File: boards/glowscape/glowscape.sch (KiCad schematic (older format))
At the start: 47 parts, among them IC1 ATMEGA168-P, IC2 SN75176B, J1 JACK_2P, J2 RJ45, J3 RJ45, J4 JACK_STEREO, SW1 SW_PUSH, SW2 SW_PUSH, SW3 SW_PUSH, X1 XO-14S

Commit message: working on routing the boards
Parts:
- added C4: 10uF, symbol C
- C1: value 2.2uF -> 100uF
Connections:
- net GND: now also C4.2
- net VCC: now also C4.1
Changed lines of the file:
@@
-EESchema Schematic File Version 2  date Mon 06 Feb 2012 02:11:49 AM EST
+EESchema Schematic File Version 2  date Fri 17 Feb 2012 09:03:31 AM EST
 LIBS:power
 LIBS:device
@@
 LIBS:xo-14s
 LIBS:diy_connectors
-EELAYER 43  0
+LIBS:glowscape-cache
+EELAYER 25  0
 EELAYER END
 $Descr A4 11700 8267
@@
 Sheet 1 1
 Title ""
-Date "6 feb 2012"
+Date "17 feb 2012"
 Rev ""
 Comp ""
@@
 Comment4 ""
 $EndDescr
+Wire Wire Line
+	4050 4850 4050 4900
 Connection ~ 3750 4550
 Wire Wire Line
@@
 	3000 1250 2850 1250
 Connection ~ 3150 1150
-Wire Wire Line
-	4050 5350 4050 5600
 Connection ~ 4050 5450
 Wire Wire Line
@@
 	4000 3750 4000 4150
 Connection ~ 4000 3750
+Wire Wire Line
+	4050 5300 4050 5600
+Connection ~ 4050 5350
+$Comp
+L C C4
+U 1 1 4F3DFEBE
+P 4050 5100
+F 0 "C4" H 4000 5200 50  0000 L CNN
+F 1 "10uF" H 3950 5000 50  0000 L CNN
+	1    4050 5100
+	1    0    0    -1
+$EndComp
+$Comp
+L VCC #PWR01
+U 1 1 4F3DFEB2
+P 4050 4850
+F 0 "#PWR01" H 4050 4950 30  0001 C CNN
+F 1 "VCC" H 4050 4950 30  0000 C CNN
+	1    4050 4850
+	1    0    0    -1
+$EndComp
 $Comp
 L JACK_STEREO J4
@@
 $EndComp
 $Comp
-L GND #PWR?
+L GND #PWR02
 U 1 1 4F2F79CC
 P 3750 4600
-F 0 "#PWR?" H 3750 4600 30  0001 C CNN
+F 0 "#PWR02" H 3750 4600 30  0001 C CNN
 F 1 "GND" H 3750 4530 30  0001 C CNN
 	1    3750 4600
@@
 $EndComp
 $Comp
-L GND #PWR?
+L GND #PWR03
 U 1 1 4F2F7860
 P 4800 2850
-F 0 "#PWR?" H 4800 2850 30  0001 C CNN
+F 0 "#PWR03" H 4800 2850 30  0001 C CNN
 F 1 "GND" H 4800 2780 30  0001 C CNN
 	1    4800 2850
@@
 $EndComp
 $Comp
-L VCC #PWR?
+L VCC #PWR04
 U 1 1 4F2F785B
 P 4800 2350
-F 0 "#PWR?" H 4800 2450 30  0001 C CNN
+F 0 "#PWR04" H 4800 2450 30  0001 C CNN
 F 1 "VCC" H 4800 2450 30  0000 C CNN
 	1    4800 2350
@@
 $EndComp
 $Comp
-L GND #PWR?
+L GND #PWR05
 U 1 1 4F2F77D5
 P 7900 5750
-F 0 "#PWR?" H 7900 5750 30  0001 C CNN
+F 0 "#PWR05" H 7900 5750 30  0001 C CNN
 F 1 "GND" H 7900 5680 30  0001 C CNN
 	1    7900 5750
@@
 $EndComp
 $Comp
-L GND #PWR?
+L GND #PWR06
 U 1 1 4F2F7745
 P 3500 5650
-F 0 "#PWR?" H 3500 5650 30  0001 C CNN
+F 0 "#PWR06" H 3500 5650 30  0001 C CNN
 F 1 "GND" H 3500 5580 30  0001 C CNN
 	1    3500 5650
@@
 $EndComp
 $Comp
-L GND #PWR?
+L GND #PWR07
 U 1 1 4F2F76AF
 P 2150 5550
-F 0 "#PWR?" H 2150 5550 30  0001 C CNN
+F 0 "#PWR07" H 2150 5550 30  0001 C CNN
 F 1 "GND" H 2150 5480 30  0001 C CNN
 	1    2150 5550
@@
 $EndComp
 $Comp
-L VCC #PWR?
+L VCC #PWR08
 U 1 1 4F2F76AC
 P 2150 4850
-F 0 "#PWR?" H 2150 4950 30  0001 C CNN
+F 0 "#PWR08" H 2150 4950 30  0001 C CNN
 F 1 "VCC" H 2150 4950 30  0000 C CNN
 	1    2150 4850
@@
 $EndComp
 $Comp
-L GND #PWR?
+L GND #PWR09
 U 1 1 4F2F7468
 P 7000 4800
-F 0 "#PWR?" H 7000 4800 30  0001 C CNN
+F 0 "#PWR09" H 7000 4800 30  0001 C CNN
 F 1 "GND" H 7000 4730 30  0001 C CNN
 	1    7000 4800
@@
 $EndComp
 $Comp
-L GND #PWR?
+L GND #PWR010
 U 1 1 4F2F6FD9
 P 6900 6200
-F 0 "#PWR?" H 6900 6200 30  0001 C CNN
+F 0 "#PWR010" H 6900 6200 30  0001 C CNN
 F 1 "GND" H 6900 6130 30  0001 C CNN
 	1    6900 6200
@@
 $EndComp
 $Comp
-L VCC #PWR?
+L VCC #PWR011
 U 1 1 4F2F6FD7
 P 6800 5650
-F 0 "#PWR?" H 6800 5750 30  0001 C CNN
+F 0 "#PWR011" H 6800 5750 30  0001 C CNN
 F 1 "VCC" H 6800 5750 30  0000 C CNN
 	1    6800 5650
@@
 $EndComp
 $Comp
-L VCC #PWR?
+L VCC #PWR012
 U 1 1 4F2F6E7B
 P 9650 3300
-F 0 "#PWR?" H 9650 3400 30  0001 C CNN
+F 0 "#PWR012" H 9650 3400 30  0001 C CNN
 F 1 "VCC" H 9650 3400 30  0000 C CNN
 	1    9650 3300
@@
 $EndComp
 $Comp
-L GND #PWR?
+L GND #PWR013
 U 1 1 4F2F6E0E
 P 7050 3350
-F 0 "#PWR?" H 7050 3350 30  0001 C CNN
+F 0 "#PWR013" H 7050 3350 30  0001 C CNN
 F 1 "GND" H 7050 3280 30  0001 C CNN
 	1    7050 3350
@@
 $EndComp
 $Comp
-L VCC #PWR?
+L VCC #PWR014
 U 1 1 4F2F6CE1
 P 7150 4050
-F 0 "#PWR?" H 7150 4150 30  0001 C CNN
+F 0 "#PWR014" H 7150 4150 30  0001 C CNN
 F 1 "VCC" H 7250 4100 30  0000 C CNN
 	1    7150 4050
@@
 $EndComp
 $Comp
-L GND #PWR?
+L GND #PWR015
 U 1 1 4F2F6CDB
 P 7050 4000
-F 0 "#PWR?" H 7050 4000 30  0001 C CNN
+F 0 "#PWR015" H 7050 4000 30  0001 C CNN
 F 1 "GND" H 7050 3930 30  0001 C CNN
 	1    7050 4000
@@
 $EndComp
 $Comp
-L GND #PWR?
+L GND #PWR016
 U 1 1 4F2F6CC9
 P 4050 5600
-F 0 "#PWR?" H 4050 5600 30  0001 C CNN
+F 0 "#PWR016" H 4050 5600 30  0001 C CNN
 F 1 "GND" H 4050 5530 30  0001 C CNN
 	1    4050 5600
@@
 $EndComp
 $Comp
-L VCC #PWR?
+L VCC #PWR017
 U 1 1 4F2F6CBC
 P 4050 3000
-F 0 "#PWR?" H 4050 3100 30  0001 C CNN
+F 0 "#PWR017" H 4050 3100 30  0001 C CNN
 F 1 "VCC" H 4050 3100 30  0000 C CNN
 	1    4050 3000
@@
 $EndComp
 $Comp
-L VCC #PWR?
+L VCC #PWR018
 U 1 1 4F2F6ACA
 P 3450 1150
-F 0 "#PWR?" H 3450 1250 30  0001 C CNN
+F 0 "#PWR018" H 3450 1250 30  0001 C CNN
 F 1 "VCC" H 3450 1250 30  0000 C CNN
 	1    3450 1150
@@
 $EndComp
 $Comp
-L GND #PWR?
+L GND #PWR019
 U 1 1 4F2F6AC6
 P 3450 1600
-F 0 "#PWR?" H 3450 1600 30  0001 C CNN
+F 0 "#PWR019" H 3450 1600 30  0001 C CNN
 F 1 "GND" H 3450 1530 30  0001 C CNN
 	1    3450 1600
@@
 P 3150 1350
 F 0 "C1" H 3200 1450 50  0000 L CNN
-F 1 "2.2uF" H 3200 1250 50  0000 L CNN
+F 1 "100uF" H 3200 1250 50  0000 L CNN
 	1    3150 1350
 	1    0    0    -1

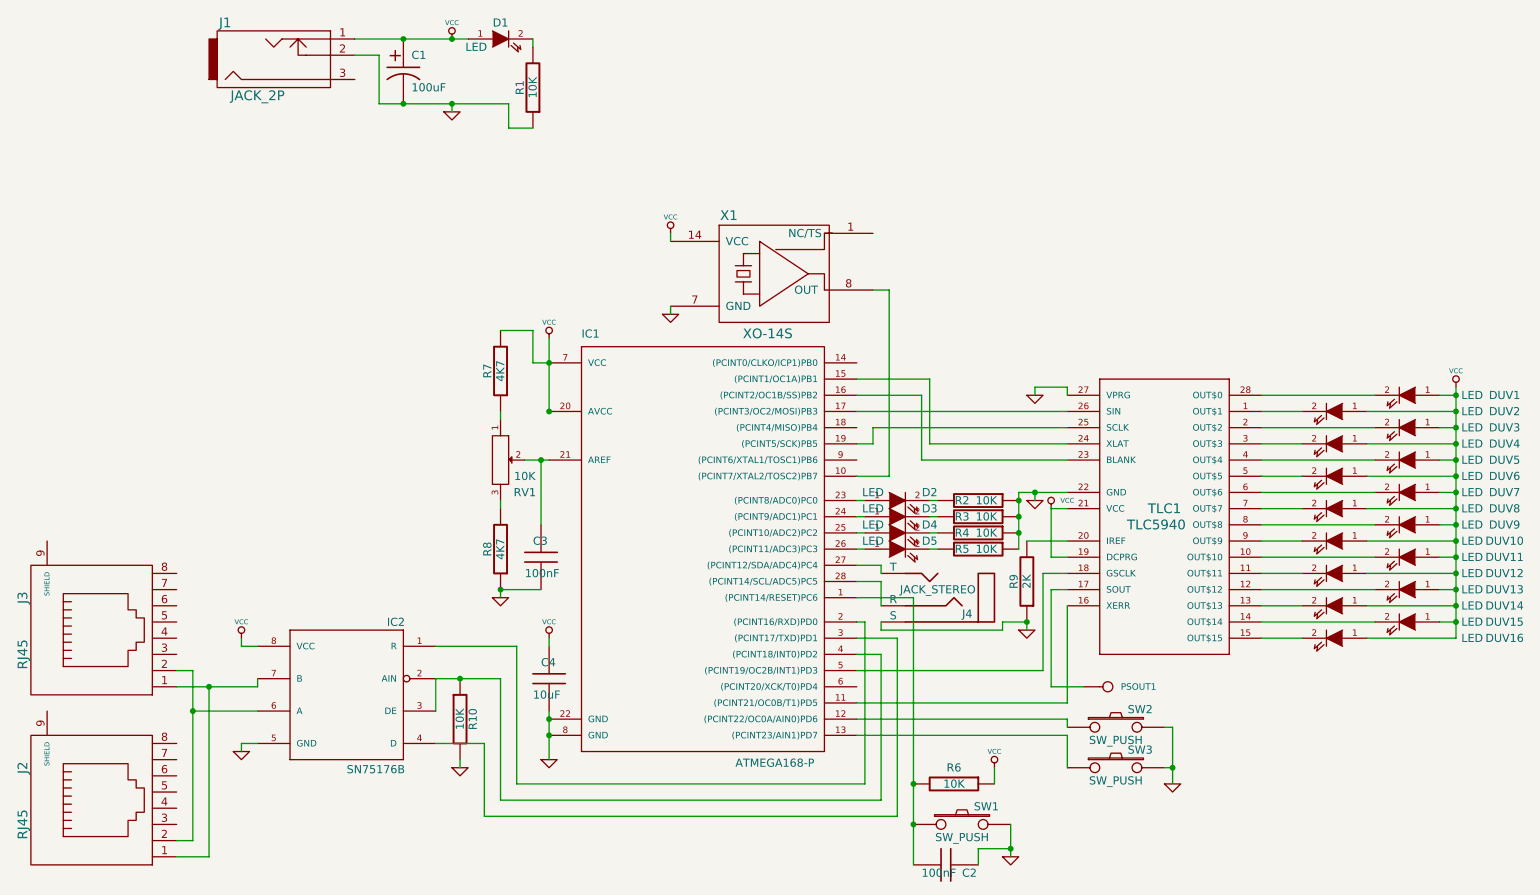
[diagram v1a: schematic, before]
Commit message: finished first board layout -- should be ready for printing
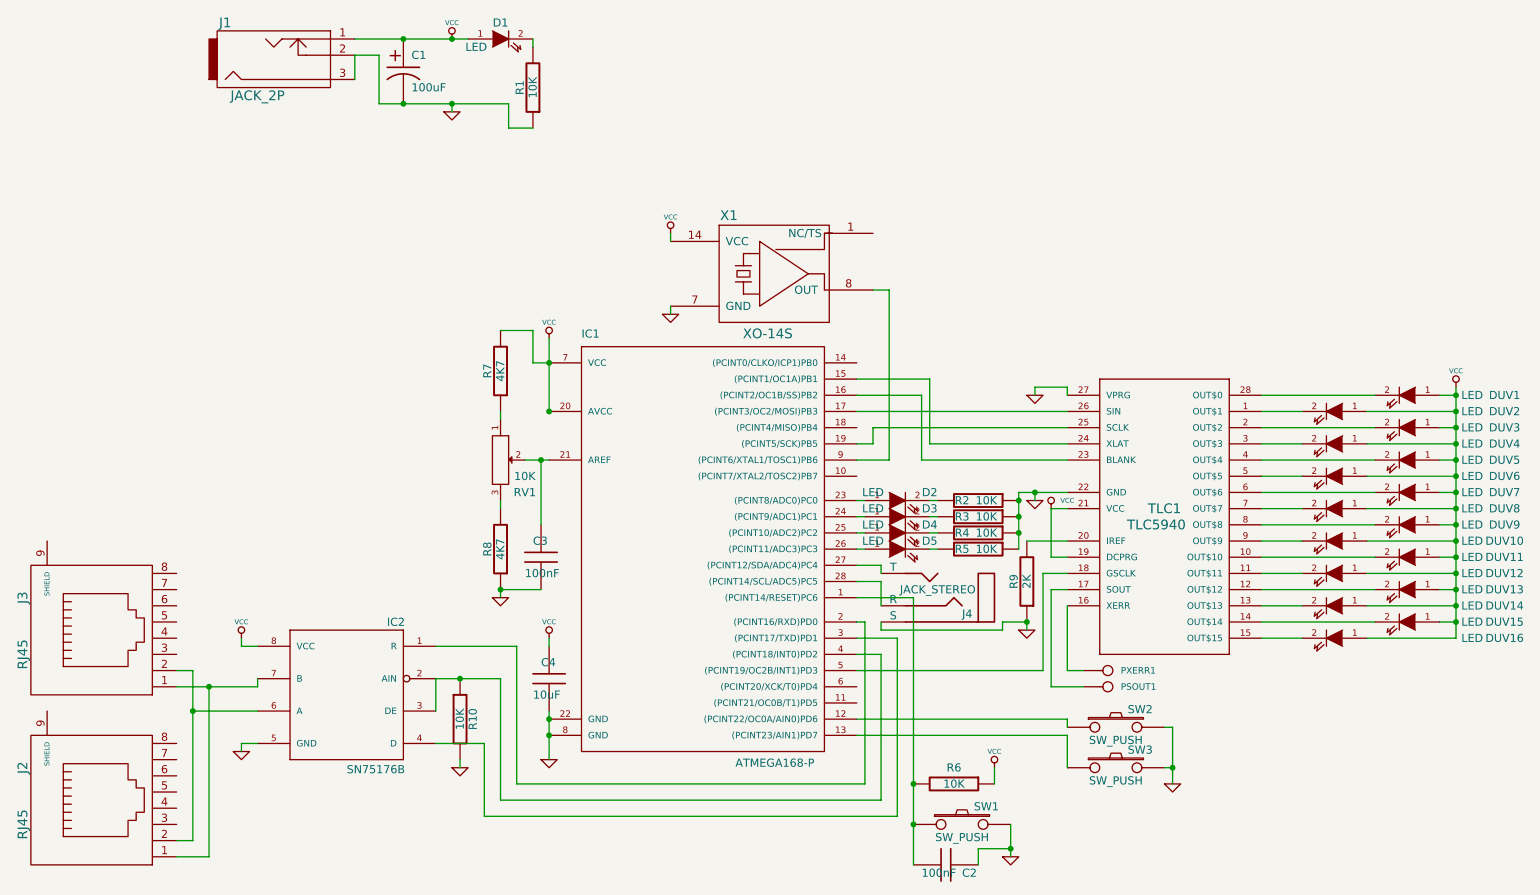
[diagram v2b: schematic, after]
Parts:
- added PXERR1: CONN_1, symbol CONN_1
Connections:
- net GND: now also J1.3
- net at IC1.10 ((PCINT7/XTAL2/TOSC2)PB7): no longer X1.8 (OUT)
- net at IC1.11 ((PCINT21/OC0B/T1)PD5): no longer TLC1.16 (XERR)
- net at IC1.9 ((PCINT6/XTAL1/TOSC1)PB6): now also X1.8 (OUT)
- new net: PXERR1.1, TLC1.16 (XERR)
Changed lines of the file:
@@
-EESchema Schematic File Version 2  date Fri 17 Feb 2012 09:03:31 AM EST
+EESchema Schematic File Version 2  date Mon 20 Feb 2012 05:59:29 AM EST
 LIBS:power
 LIBS:device
@@
 Sheet 1 1
 Title ""
-Date "17 feb 2012"
+Date "20 feb 2012"
 Rev ""
 Comp ""
@@
 $EndDescr
 Wire Wire Line
+	2850 1400 2850 1250
+Wire Wire Line
+	5950 3750 6150 3750
+Wire Wire Line
+	6150 3750 6150 2700
+Wire Wire Line
 	4050 4850 4050 4900
 Connection ~ 3750 4550
@@
 	6400 4000 6450 4000
 Wire Wire Line
-	5950 5250 7250 5250
-Wire Wire Line
 	5950 3450 7250 3450
 Wire Wire Line
@@
 Connection ~ 3450 1150
 Wire Wire Line
-	2850 1150 3550 1150
+	3550 1150 2850 1150
 Connection ~ 3450 1550
 Wire Wire Line
@@
 	6300 6250 6300 4600
 Wire Wire Line
-	6900 6000 6900 6200
+	6900 6200 6900 6000
 Wire Wire Line
 	9650 4550 9550 4550
@@
 	6050 3650 5950 3650
 Wire Wire Line
-	6050 2700 6150 2700
-Wire Wire Line
-	6150 2700 6150 3850
-Wire Wire Line
-	6150 3850 5950 3850
+	6150 2700 6050 2700
 Connection ~ 3150 1550
 Wire Wire Line
@@
 	7250 4450 7100 4450
 Wire Wire Line
-	7250 5250 7250 4650
-Wire Wire Line
 	7250 3350 7250 3300
 Wire Wire Line
@@
 	4800 2400 4800 2350
 Wire Wire Line
-	3900 3750 4050 3750
-Wire Wire Line
-	4050 3000 4050 3450
+	4050 3750 3900 3750
+Wire Wire Line
+	4050 3450 4050 3000
 Connection ~ 4050 3150
 Wire Wire Line
@@
 	6100 4500 5950 4500
 Wire Wire Line
-	4000 3750 4000 4150
+	4000 4150 4000 3750
 Connection ~ 4000 3750
 Wire Wire Line
-	4050 5300 4050 5600
+	4050 5600 4050 5300
 Connection ~ 4050 5350
+Wire Wire Line
+	7250 4650 7250 5050
+Wire Wire Line
+	7250 5050 7350 5050
+$Comp
+L CONN_1 PXERR1
+U 1 1 4F41B10C
+P 7500 5050
+F 0 "PXERR1" H 7580 5050 40  0000 L CNN
+F 1 "CONN_1" H 7500 5105 30  0001 C CNN
+	1    7500 5050
+	1    0    0    -1
+$EndComp
 $Comp
 L C C4
@@
 $EndComp
 $Comp
-L VCC #PWR01
+L VCC #PWR02
 U 1 1 4F3DFEB2
 P 4050 4850
-F 0 "#PWR01" H 4050 4950 30  0001 C CNN
+F 0 "#PWR02" H 4050 4950 30  0001 C CNN
 F 1 "VCC" H 4050 4950 30  0000 C CNN
 	1    4050 4850
@@
 $EndComp
 $Comp
-L GND #PWR02
+L GND #PWR03
 U 1 1 4F2F79CC
 P 3750 4600
-F 0 "#PWR02" H 3750 4600 30  0001 C CNN
+F 0 "#PWR03" H 3750 4600 30  0001 C CNN
 F 1 "GND" H 3750 4530 30  0001 C CNN
 	1    3750 4600
@@
 $EndComp
 $Comp
-L GND #PWR03
+L GND #PWR04
 U 1 1 4F2F7860
 P 4800 2850
-F 0 "#PWR03" H 4800 2850 30  0001 C CNN
+F 0 "#PWR04" H 4800 2850 30  0001 C CNN
 F 1 "GND" H 4800 2780 30  0001 C CNN
 	1    4800 2850
@@
 $EndComp
 $Comp
-L VCC #PWR04
+L VCC #PWR05
 U 1 1 4F2F785B
 P 4800 2350
-F 0 "#PWR04" H 4800 2450 30  0001 C CNN
+F 0 "#PWR05" H 4800 2450 30  0001 C CNN
 F 1 "VCC" H 4800 2450 30  0000 C CNN
 	1    4800 2350
@@
 $EndComp
 $Comp
-L GND #PWR05
+L GND #PWR06
 U 1 1 4F2F77D5
 P 7900 5750
-F 0 "#PWR05" H 7900 5750 30  0001 C CNN
+F 0 "#PWR06" H 7900 5750 30  0001 C CNN
 F 1 "GND" H 7900 5680 30  0001 C CNN
 	1    7900 5750
@@
 $EndComp
 $Comp
-L GND #PWR06
+L GND #PWR07
 U 1 1 4F2F7745
 P 3500 5650
-F 0 "#PWR06" H 3500 5650 30  0001 C CNN
+F 0 "#PWR07" H 3500 5650 30  0001 C CNN
 F 1 "GND" H 3500 5580 30  0001 C CNN
 	1    3500 5650
@@
 $EndComp
 $Comp
-L GND #PWR07
+L GND #PWR08
 U 1 1 4F2F76AF
 P 2150 5550
-F 0 "#PWR07" H 2150 5550 30  0001 C CNN
+F 0 "#PWR08" H 2150 5550 30  0001 C CNN
 F 1 "GND" H 2150 5480 30  0001 C CNN
 	1    2150 5550
@@
 $EndComp
 $Comp
-L VCC #PWR08
+L VCC #PWR09
 U 1 1 4F2F76AC
 P 2150 4850
-F 0 "#PWR08" H 2150 4950 30  0001 C CNN
+F 0 "#PWR09" H 2150 4950 30  0001 C CNN
 F 1 "VCC" H 2150 4950 30  0000 C CNN
 	1    2150 4850
@@
 $EndComp
 $Comp
-L GND #PWR09
+L GND #PWR010
 U 1 1 4F2F7468
 P 7000 4800
-F 0 "#PWR09" H 7000 4800 30  0001 C CNN
+F 0 "#PWR010" H 7000 4800 30  0001 C CNN
 F 1 "GND" H 7000 4730 30  0001 C CNN
 	1    7000 4800
@@
 $EndComp
 $Comp
-L GND #PWR010
+L GND #PWR011
 U 1 1 4F2F6FD9
 P 6900 6200
-F 0 "#PWR010" H 6900 6200 30  0001 C CNN
+F 0 "#PWR011" H 6900 6200 30  0001 C CNN
 F 1 "GND" H 6900 6130 30  0001 C CNN
 	1    6900 6200
@@
 $EndComp
 $Comp
-L VCC #PWR011
+L VCC #PWR012
 U 1 1 4F2F6FD7
 P 6800 5650
-F 0 "#PWR011" H 6800 5750 30  0001 C CNN
+F 0 "#PWR012" H 6800 5750 30  0001 C CNN
 F 1 "VCC" H 6800 5750 30  0000 C CNN
 	1    6800 5650
@@
 $EndComp
 $Comp
-L VCC #PWR012
+L VCC #PWR013
 U 1 1 4F2F6E7B
 P 9650 3300
-F 0 "#PWR012" H 9650 3400 30  0001 C CNN
+F 0 "#PWR013" H 9650 3400 30  0001 C CNN
 F 1 "VCC" H 9650 3400 30  0000 C CNN
 	1    9650 3300
@@
 $EndComp
 $Comp
-L GND #PWR013
+L GND #PWR014
 U 1 1 4F2F6E0E
 P 7050 3350
-F 0 "#PWR013" H 7050 3350 30  0001 C CNN
+F 0 "#PWR014" H 7050 3350 30  0001 C CNN
 F 1 "GND" H 7050 3280 30  0001 C CNN
 	1    7050 3350
@@
 $EndComp
 $Comp
-L VCC #PWR014
+L VCC #PWR015
 U 1 1 4F2F6CE1
 P 7150 4050
-F 0 "#PWR014" H 7150 4150 30  0001 C CNN
+F 0 "#PWR015" H 7150 4150 30  0001 C CNN
 F 1 "VCC" H 7250 4100 30  0000 C CNN
 	1    7150 4050
@@
 $EndComp
 $Comp
-L GND #PWR015
+L GND #PWR016
 U 1 1 4F2F6CDB
 P 7050 4000
-F 0 "#PWR015" H 7050 4000 30  0001 C CNN
+F 0 "#PWR016" H 7050 4000 30  0001 C CNN
 F 1 "GND" H 7050 3930 30  0001 C CNN
 	1    7050 4000
@@
 $EndComp
 $Comp
-L GND #PWR016
+L GND #PWR017
 U 1 1 4F2F6CC9
 P 4050 5600
-F 0 "#PWR016" H 4050 5600 30  0001 C CNN
+F 0 "#PWR017" H 4050 5600 30  0001 C CNN
 F 1 "GND" H 4050 5530 30  0001 C CNN
 	1    4050 5600
@@
 $EndComp
 $Comp
-L VCC #PWR017
+L VCC #PWR018
 U 1 1 4F2F6CBC
 P 4050 3000
-F 0 "#PWR017" H 4050 3100 30  0001 C CNN
+F 0 "#PWR018" H 4050 3100 30  0001 C CNN
 F 1 "VCC" H 4050 3100 30  0000 C CNN
 	1    4050 3000
@@
 $EndComp
 $Comp
-L VCC #PWR018
+L VCC #PWR019
 U 1 1 4F2F6ACA
 P 3450 1150
-F 0 "#PWR018" H 3450 1250 30  0001 C CNN
+F 0 "#PWR019" H 3450 1250 30  0001 C CNN
 F 1 "VCC" H 3450 1250 30  0000 C CNN
 	1    3450 1150
@@
 $EndComp
 $Comp
-L GND #PWR019
+L GND #PWR020
 U 1 1 4F2F6AC6
 P 3450 1600
-F 0 "#PWR019" H 3450 1600 30  0001 C CNN
+F 0 "#PWR020" H 3450 1600 30  0001 C CNN
 F 1 "GND" H 3450 1530 30  0001 C CNN
 	1    3450 1600
